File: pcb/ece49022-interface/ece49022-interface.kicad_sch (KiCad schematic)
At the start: 4 parts, among them J1 Conn_01x02_Pin

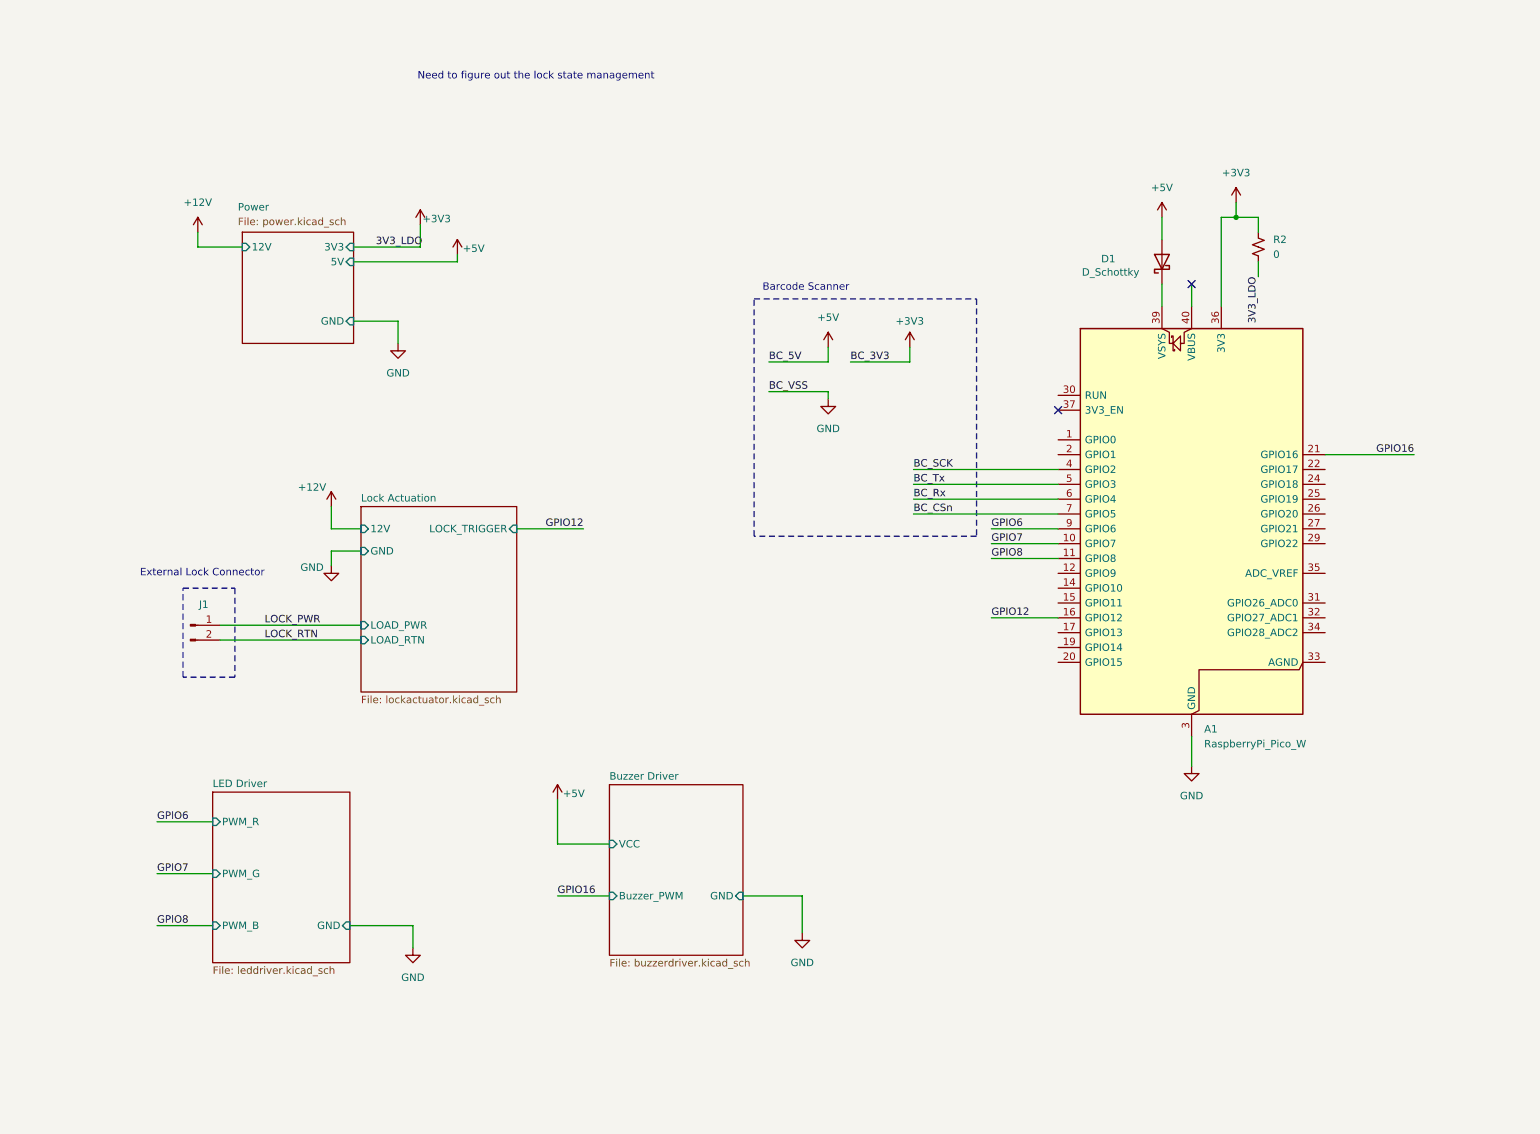
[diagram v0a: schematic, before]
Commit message: Fingerprint Scanner
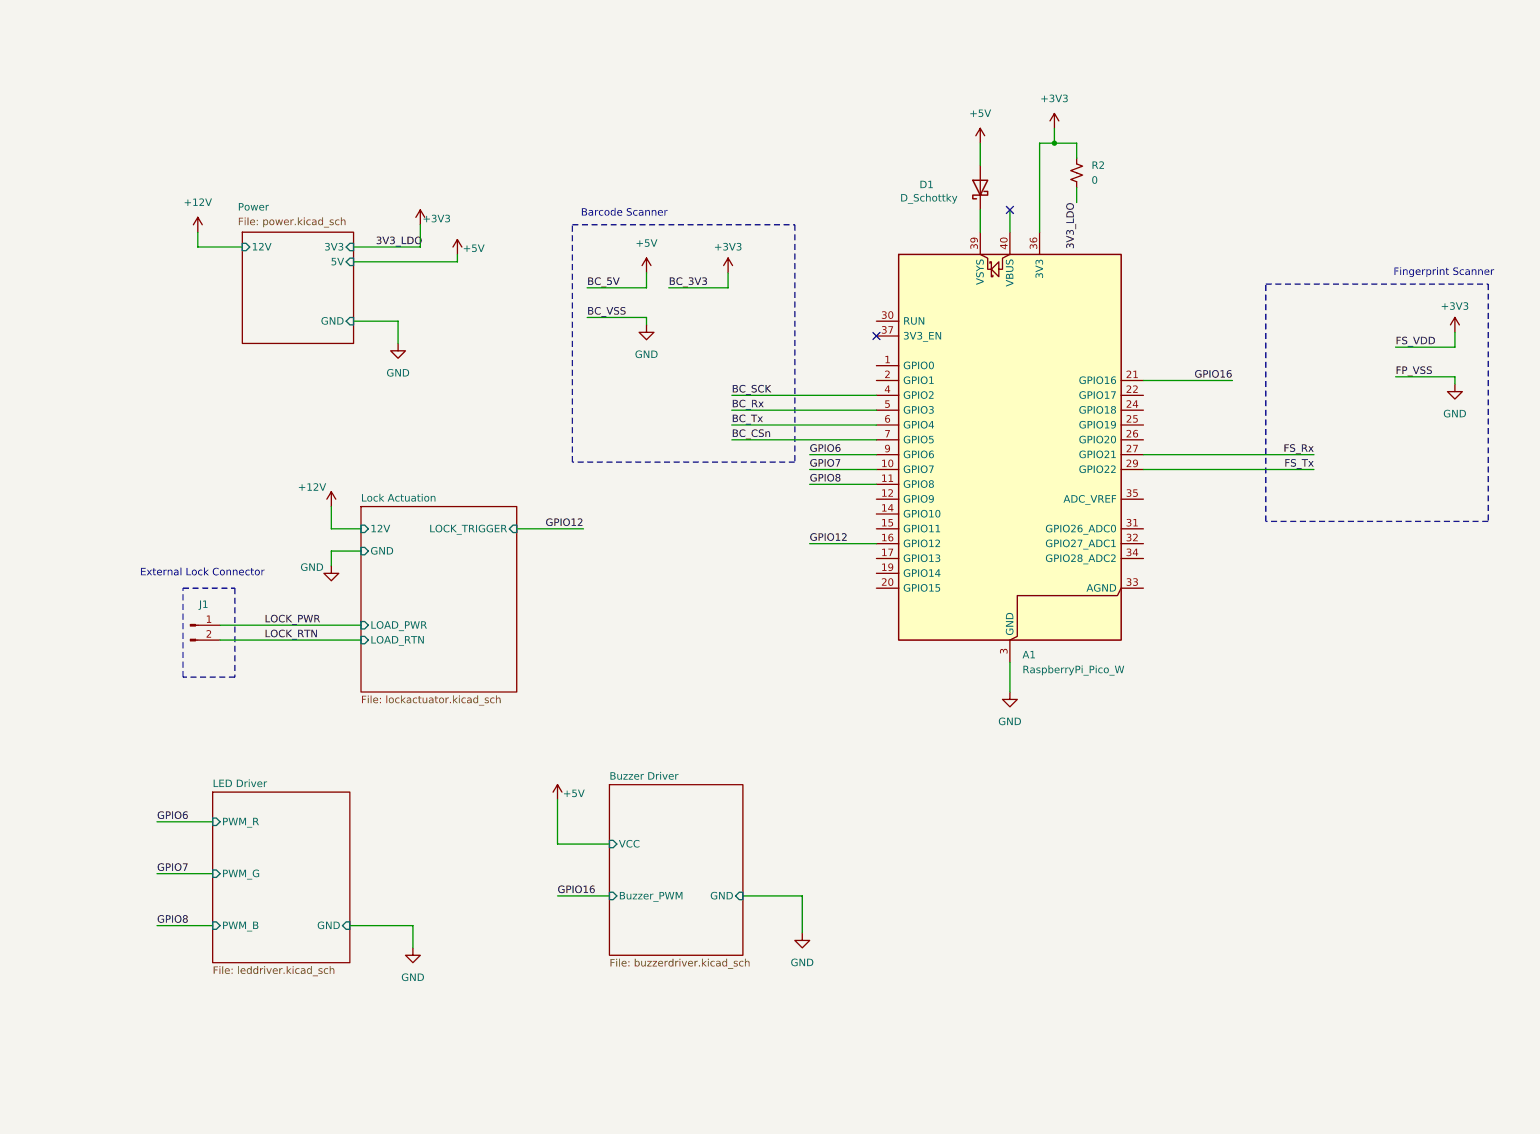
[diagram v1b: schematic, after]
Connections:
- net BC_Rx: now also A1.5 (GPIO3); no longer A1.6 (GPIO4)
- net BC_Tx: now also A1.6 (GPIO4); no longer A1.5 (GPIO3)
- net FS_Rx: now reaches A1.27 (GPIO21)
- net FS_Tx: now reaches A1.29 (GPIO22)
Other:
- note added: "Fingerprint Scanner"
- note removed: "Need to figure out the lock state management"
- moved on the sheet: A1, D1, R2

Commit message: Update ece49022-interface.kicad_sch
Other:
- note added: "Need to figure out the lock state management"
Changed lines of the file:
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@@
+		)
+	)
+	(text "Need to figure out the lock state management\n"
+		(exclude_from_sim no)
+		(at 107.442 16.51 0)
+		(effects
+			(font
+				(size 1.27 1.27)
+			)
 		)
 	)

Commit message: footprint update
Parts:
- removed R2: 0, symbol Device:R_Small_US
- D1: footprint (none) -> Diode_SMD:D_2114_3652Metric_Pad1.85x3.75mm_HandSolder
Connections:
- net +3V3: no longer A1.36 (3V3)
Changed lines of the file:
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@@
 		)
-	)
-	(junction
-		(at 196.215 27.94)
-		(diameter 0)
-		(color 0 0 0 0)
 	)
 	(no_connect
@@
 	(wire
 		(pts
-			(xy 196.215 27.94) (xy 200.025 27.94)
-		)
-		(stroke
-			(width 0)
-			(type default)
-		)
-	)
-	(wire
-		(pts
 			(xy 75.565 161.925) (xy 86.36 161.925)
 		)
@@
 	(wire
 		(pts
-			(xy 196.215 27.94) (xy 193.675 27.94)
-		)
-		(stroke
-			(width 0)
-			(type default)
-		)
-	)
-	(wire
-		(pts
 			(xy 111.125 147.955) (xy 120.015 147.955)
 		)
@@
 	(wire
 		(pts
-			(xy 200.025 35.56) (xy 200.025 38.1)
-		)
-		(stroke
-			(width 0)
-			(type default)
-		)
-	)
-	(wire
-		(pts
 			(xy 140.97 73.66) (xy 165.735 73.66)
 		)
@@
 	(wire
 		(pts
-			(xy 196.215 25.4) (xy 196.215 27.94)
-		)
-		(stroke
-			(width 0)
-			(type default)
-		)
-	)
-	(wire
-		(pts
 			(xy 42.545 153.035) (xy 52.07 153.035)
 		)
@@
 	(wire
 		(pts
-			(xy 200.025 27.94) (xy 200.025 30.48)
-		)
-		(stroke
-			(width 0)
-			(type default)
-		)
-	)
-	(wire
-		(pts
 			(xy 116.205 57.785) (xy 126.365 57.785)
 		)
@@
 		(pts
 			(xy 116.205 52.705) (xy 126.365 52.705)
-		)
-		(stroke
-			(width 0)
-			(type default)
-		)
-	)
-	(wire
-		(pts
-			(xy 193.675 27.94) (xy 193.675 43.18)
 		)
 		(stroke
@@
 			)
 			(justify left bottom)
-		)
-	)
-	(label "3V3_LDO"
-		(at 200.025 38.1 270)
-		(effects
-			(font
-				(size 1.27 1.27)
-			)
-			(justify right bottom)
 		)
 	)
@@
 	(symbol
 		(lib_id "power:+3V3")
-		(at 196.215 25.4 0)
-		(unit 1)
-		(exclude_from_sim no)
-		(in_bom yes)
-		(on_board yes)
-		(dnp no)
-		(fields_autoplaced yes)
-		(property "Reference" "#PWR045"
-			(at 196.215 29.21 0)
-			(effects
-				(font
-					(size 1.27 1.27)
-				)
-				(hide yes)
-			)
-		)
-		(property "Value" "+3V3"
-			(at 196.215 20.32 0)
-			(effects
-				(font
-					(size 1.27 1.27)
-				)
-			)
-		)
-		(property "Footprint" ""
-			(at 196.215 25.4 0)
-			(effects
-				(font
-					(size 1.27 1.27)
-				)
-				(hide yes)
-			)
-		)
-		(property "Datasheet" ""
-			(at 196.215 25.4 0)
-			(effects
-				(font
-					(size 1.27 1.27)
-				)
-				(hide yes)
-			)
-		)
-		(property "Description" "Power symbol creates a global label with name \"+3V3\""
-			(at 196.215 25.4 0)
-			(effects
-				(font
-					(size 1.27 1.27)
-				)
-				(hide yes)
-			)
-		)
-		(pin "1"
-		)
-		(instances
-			(project "ece49022-interface"
-				(path "/ad062fbe-cbe6-4ffd-876d-97a59a1c7176"
-					(reference "#PWR045")
-					(unit 1)
-				)
-			)
-		)
-	)
-	(symbol
-		(lib_id "power:+3V3")
 		(at 183.515 27.94 0)
 		(unit 1)
@@
 	)
 	(symbol
-		(lib_id "Device:R_Small_US")
-		(at 200.025 33.02 0)
-		(unit 1)
-		(exclude_from_sim no)
-		(in_bom yes)
-		(on_board yes)
-		(dnp no)
-		(fields_autoplaced yes)
-		(property "Reference" "R2"
-			(at 202.565 31.7499 0)
-			(effects
-				(font
-					(size 1.27 1.27)
-				)
-				(justify left)
-			)
-		)
-		(property "Value" "0"
-			(at 202.565 34.2899 0)
-			(effects
-				(font
-					(size 1.27 1.27)
-				)
-				(justify left)
-			)
-		)
-		(property "Footprint" ""
-			(at 200.025 33.02 0)
-			(effects
-				(font
-					(size 1.27 1.27)
-				)
-				(hide yes)
-			)
-		)
-		(property "Datasheet" "~"
-			(at 200.025 33.02 0)
-			(effects
-				(font
-					(size 1.27 1.27)
-				)
-				(hide yes)
-			)
-		)
-		(property "Description" "Resistor, small US symbol"
-			(at 200.025 33.02 0)
-			(effects
-				(font
-					(size 1.27 1.27)
-				)
-				(hide yes)
-			)
-		)
-		(pin "1"
-		)
-		(pin "2"
-		)
-		(instances
-			(project ""
-				(path "/ad062fbe-cbe6-4ffd-876d-97a59a1c7176"
-					(reference "R2")
-					(unit 1)
-				)
-			)
-		)
-	)
-	(symbol
 		(lib_id "power:GND")
 		(at 72.39 100.33 0)
@@
 			)
 		)
-		(property "Footprint" ""
+		(property "Footprint" "Diode_SMD:D_2114_3652Metric_Pad1.85x3.75mm_HandSolder"
 			(at 183.515 35.56 0)
 			(effects

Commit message: start pcb
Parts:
- J1: footprint (none) -> Connector_PinHeader_2.54mm:PinHeader_1x02_P2.54mm_Vertical
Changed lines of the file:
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@@
+	)
+	(symbol
+		(lib_id "Connector:Conn_01x02_Pin")
+		(at 48.26 110.49 0)
+		(unit 1)
+		(exclude_from_sim no)
+		(in_bom yes)
+		(on_board yes)
+		(dnp no)
+		(property "Reference" "J1"
+			(at 48.768 107.442 0)
+			(effects
+				(font
+					(size 1.27 1.27)
+				)
+			)
+		)
+		(property "Value" "Conn_01x02_Pin"
+			(at 48.895 107.95 0)
+			(effects
+				(font
+					(size 1.27 1.27)
+				)
+				(hide yes)
+			)
+		)
+		(property "Footprint" "Connector_PinHeader_2.54mm:PinHeader_1x02_P2.54mm_Vertical"
+			(at 48.26 110.49 0)
+			(effects
+				(font
+					(size 1.27 1.27)
+				)
+				(hide yes)
+			)
+		)
+		(property "Datasheet" "~"
+			(at 48.26 110.49 0)
+			(effects
+				(font
+					(size 1.27 1.27)
+				)
+				(hide yes)
+			)
+		)
+		(property "Description" "Generic connector, single row, 01x02, script generated"
+			(at 48.26 110.49 0)
+			(effects
+				(font
+					(size 1.27 1.27)
+				)
+				(hide yes)
+			)
+		)
+		(pin "2"
+		)
+		(pin "1"
+		)
+		(instances
+			(project "ece49022-interface"
+				(path "/ad062fbe-cbe6-4ffd-876d-97a59a1c7176"
+					(reference "J1")
+					(unit 1)
+				)
+			)
+		)
 	)
 	(symbol
@@
 					(unit 1)
 				)
-			)
-		)
-	)
-	(symbol
-		(lib_id "Connector:Conn_01x02_Pin")
-		(at 48.26 110.49 0)
-		(unit 1)
-		(exclude_from_sim no)
-		(in_bom yes)
-		(on_board yes)
-		(dnp no)
-		(property "Reference" "J1"
-			(at 50.546 106.934 0)
-			(effects
-				(font
-					(size 1.27 1.27)
-				)
-			)
-		)
-		(property "Value" "Conn_01x02_Pin"
-			(at 44.45 107.95 0)
-			(effects
-				(font
-					(size 1.27 1.27)
-				)
-				(hide yes)
-			)
-		)
-		(property "Footprint" ""
-			(at 48.26 110.49 0)
-			(effects
-				(font
-					(size 1.27 1.27)
-				)
-				(hide yes)
-			)
-		)
-		(property "Datasheet" "~"
-			(at 48.26 110.49 0)
-			(effects
-				(font
-					(size 1.27 1.27)
-				)
-				(hide yes)
-			)
-		)
-		(property "Description" "Generic connector, single row, 01x02, script generated"
-			(at 48.26 110.49 0)
-			(effects
-				(font
-					(size 1.27 1.27)
-				)
-				(hide yes)
-			)
-		)
-		(pin "1"
-		)
-		(pin "2"
-		)
-		(instances
-			(project ""
-				(path "/ad062fbe-cbe6-4ffd-876d-97a59a1c7176"
-					(reference "J1")
-					(unit 1)
-				)

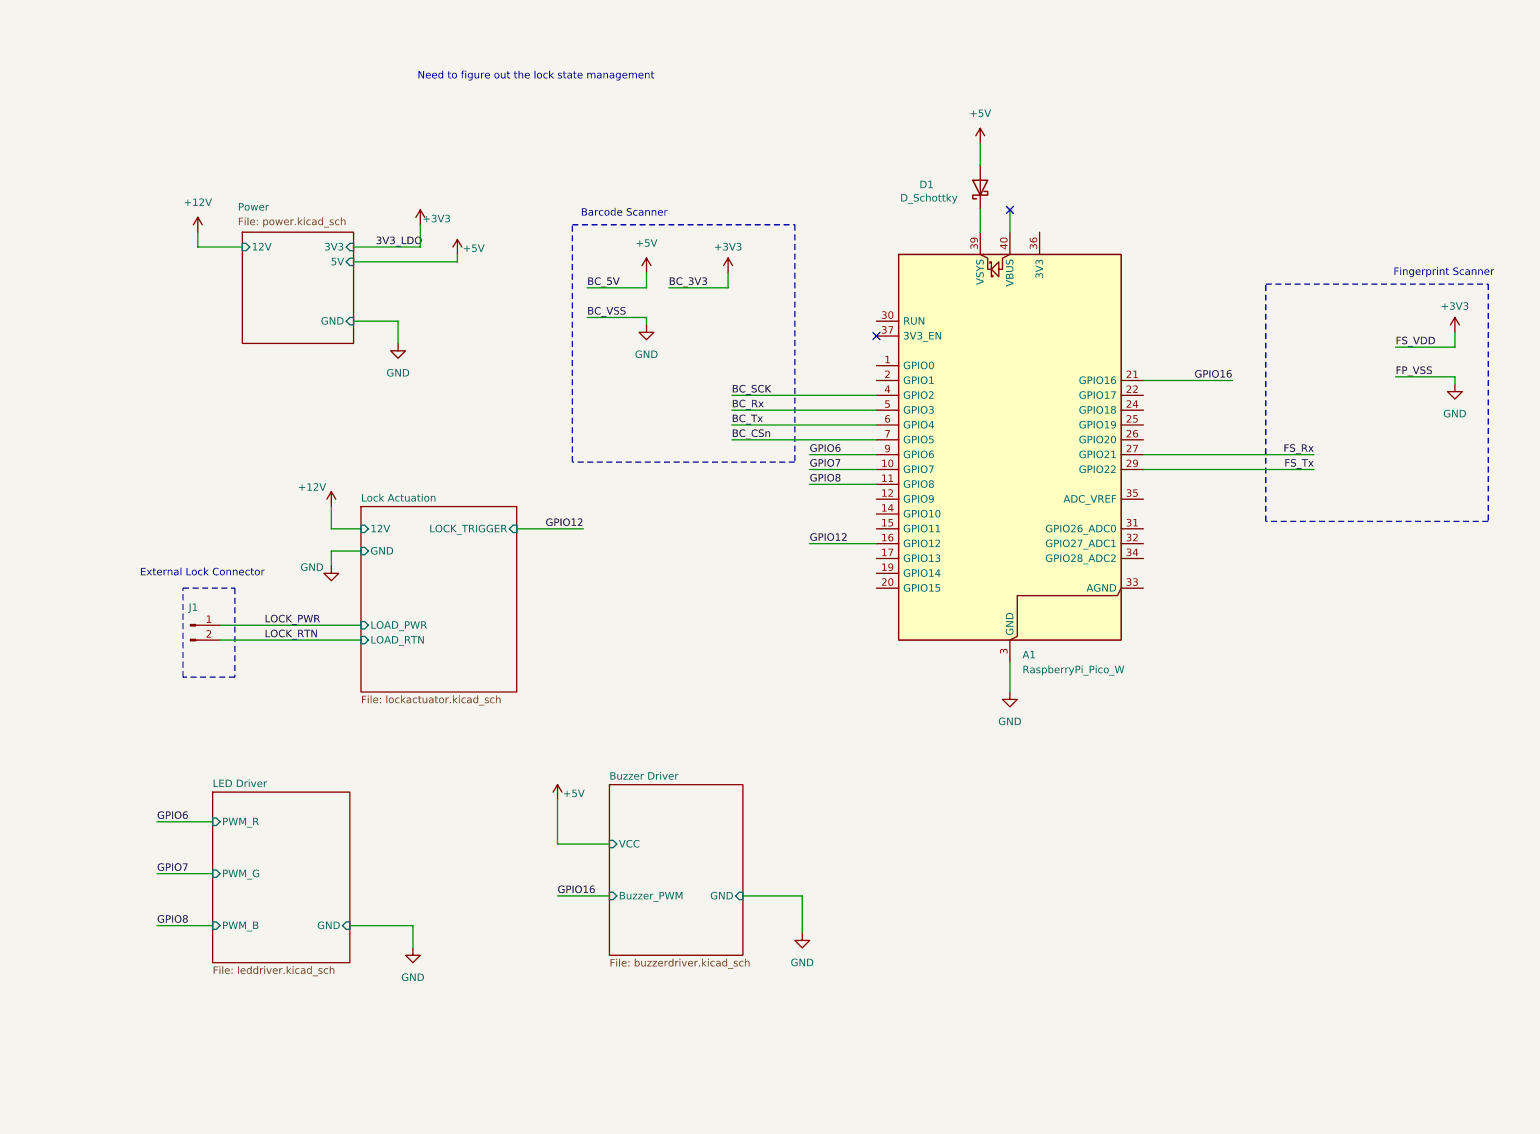
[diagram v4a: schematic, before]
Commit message: Add pin connectors
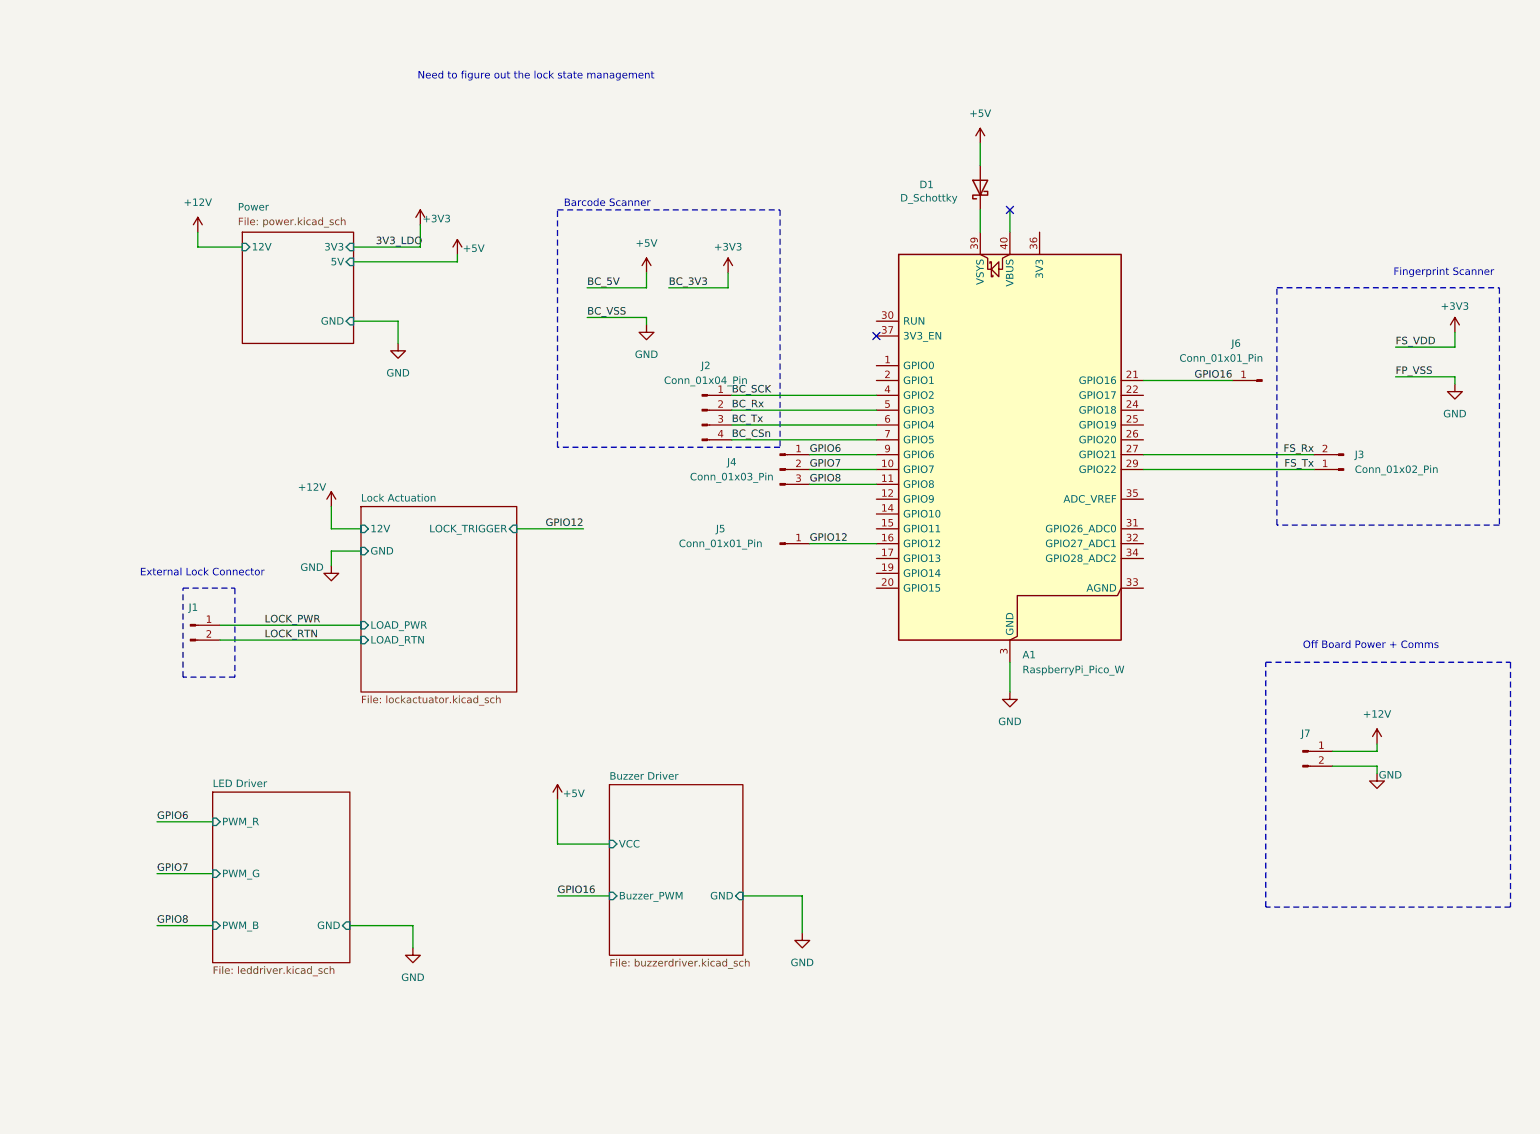
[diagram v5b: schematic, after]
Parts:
- added J2: Conn_01x04_Pin, Connector_PinHeader_2.54mm:PinHeader_1x04_P2.54mm_Vertical, symbol Connector:Conn_01x04_Pin
- added J3: Conn_01x02_Pin, Connector_PinHeader_2.54mm:PinHeader_1x02_P2.54mm_Vertical, symbol Connector:Conn_01x02_Pin
- added J4: Conn_01x03_Pin, Connector_PinHeader_2.54mm:PinHeader_1x03_P2.54mm_Vertical, symbol Connector:Conn_01x03_Pin
- added J5, J6: Conn_01x01_Pin, Connector_PinHeader_2.54mm:PinHeader_1x01_P2.54mm_Vertical, symbol Connector:Conn_01x01_Pin
- renumbered J1 to J7
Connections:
- net +12V: now also J7.1 (Pin_1)
- net BC_CSn: now also J2.4 (Pin_4)
- net BC_Rx: now also J2.2 (Pin_2)
- net BC_SCK: now also J2.1 (Pin_1)
- net BC_Tx: now also J2.3 (Pin_3)
- net FS_Rx: now also J3.2 (Pin_2)
- net FS_Tx: now also J3.1 (Pin_1)
- net GND: now also J7.2 (Pin_2)
- net GPIO12: now also J5.1 (Pin_1)
- net GPIO16: now also J6.1 (Pin_1)
- net GPIO6: now also J4.1 (Pin_1)
- net GPIO7: now also J4.2 (Pin_2)
- net GPIO8: now also J4.3 (Pin_3)
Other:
- note added: "Off Board Power + Comms"
